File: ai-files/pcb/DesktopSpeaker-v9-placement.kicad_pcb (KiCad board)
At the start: 4 copper layers, 136.9 x 127.8 mm, 351 parts, among them J1 USB_C_Receptacle_USB2.0_16P, J10 B2P-VH, J11 B2P-VH, J2 HEAD_OUT, J3 AUX_IN, J4 I2C service, J5 1S_PACK_3PIN, J6 SWD, J7 SWD_TC2030, J8 BM83_PROG, J9 B2P-VH, Q100 2N7002, Q101 2N7002, Q102 2N7002, Q103 CSD17579Q3A, Q104 2N7002, SW100 WAKE_QON, SW101 BAT_DISCONNECT, SW102 EC11E, U1 BM83SM1-00TA, U10 TPA6132A2RTER, U11 TPS25730DREFR, U12 TPS7A0230PDBVR, U13 TS5A3167DBVR, U14 TPS63802DLAR, U15 TPS63802DLAR, U16 TS5A3167DBVR, U17 TS5A3167DBVR, U19 TPS7B8450QWDRBRQ1, U2 PCM2902CDBR, U20 TPS2116DRLR, U21 TPS3839G33DBZR, U22 TPS7A2033PDBVR, U23 TPS22917DBVR, U24 PCM1862DBTR, U25 TPS61088RHLR, U3 STM32G071RBT6, U4 BQ25792RQMR, U5 MAX17048G+T10, U6 TAS5825MRHBR, U7 TAS5825MRHBR, U8 TS5A23157DGSR, U9 TS5A23157DGSR, Y170 12MHz, Y200 24.576MHz

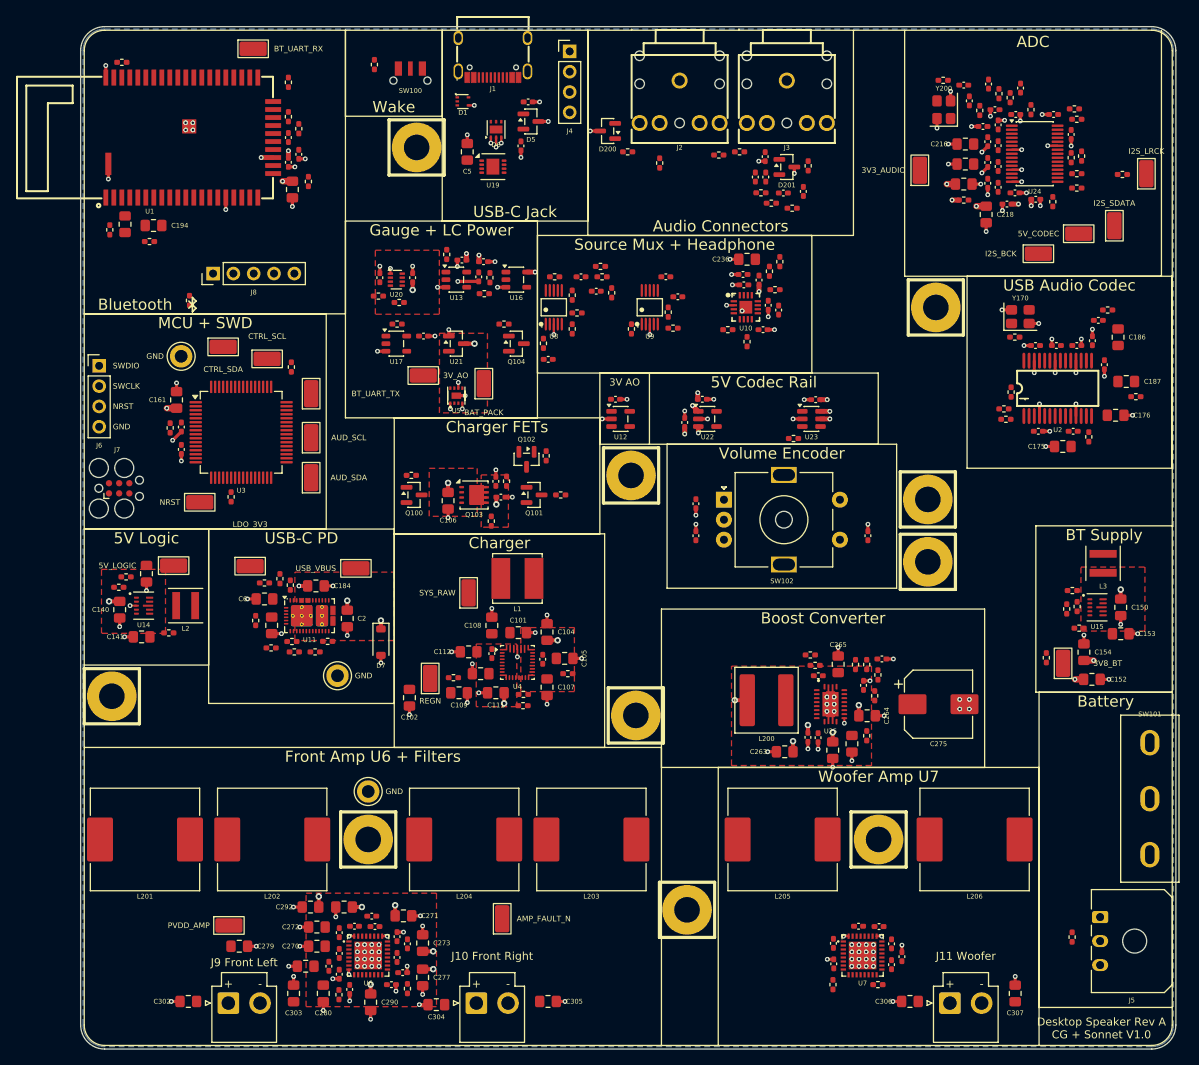
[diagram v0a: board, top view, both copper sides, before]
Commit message: Routing phase 0: GND planes, In2 rail islands, F.Cu pours, 203 GND vias, rail vias; Freerouting trial (draft, not adopted); routing P0 scripts and report
Co-Authored-By: Claude Sonnet 5.5 <noreply@anthropic.com>
Claude-Session: https://claude.ai/code/session_016fe4xPJbEE2SjGafuyNLjb
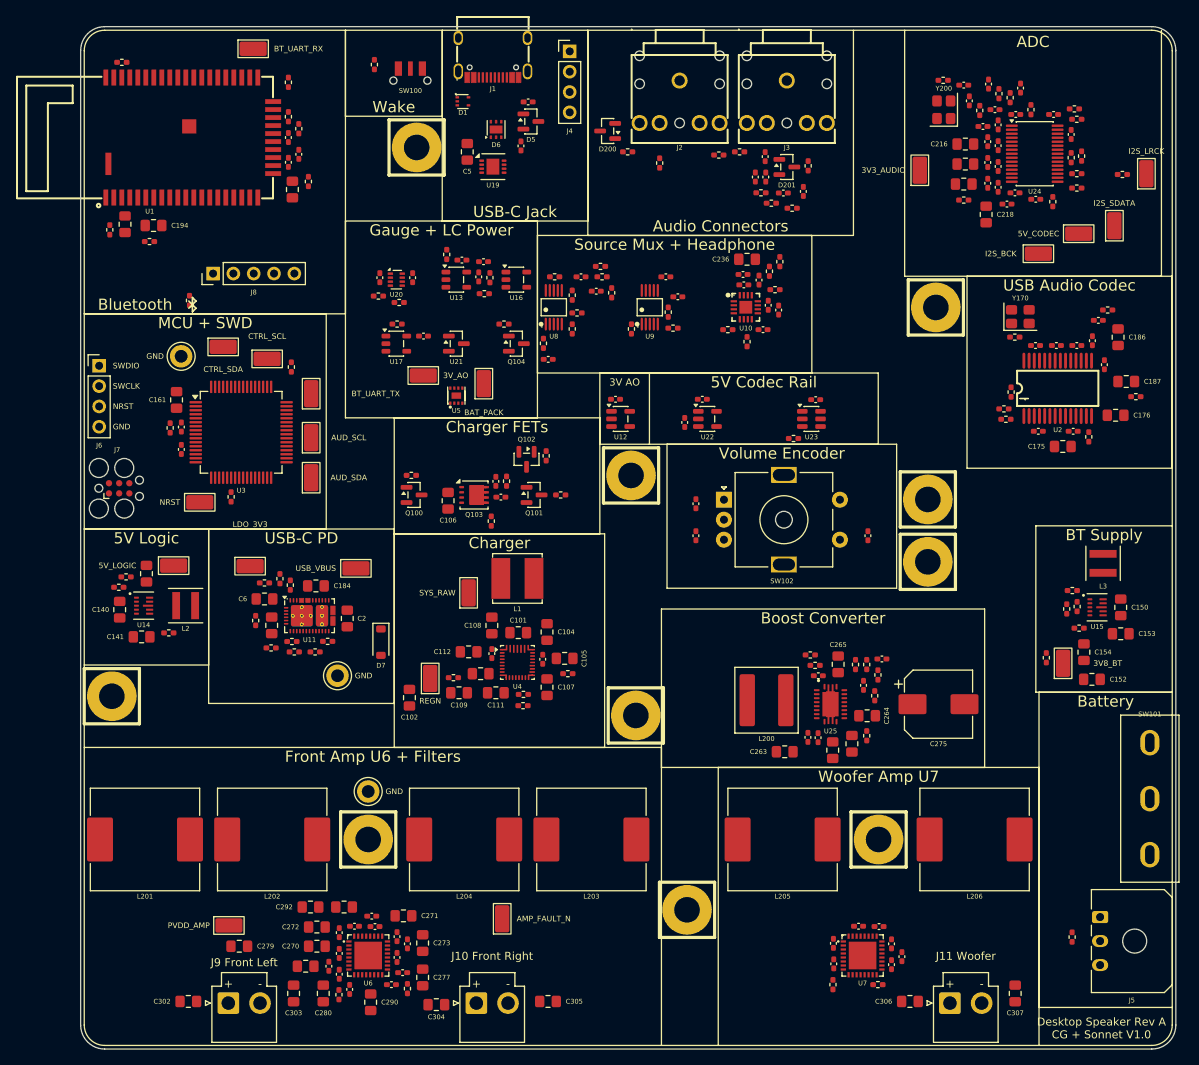
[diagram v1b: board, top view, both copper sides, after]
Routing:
- net GND: track 159.0 -> 0.00 mm, vias 203 -> 0
- net /SYS_RAW: track 11.2 -> 0.00 mm, vias 9 -> 0
- net /Amplifiers/PVDD_AMP: track 7.68 -> 0.00 mm, vias 6 -> 0
- net /3V8_BT: track 5.90 -> 0.00 mm, vias 5 -> 0
- net /3V3_AUDIO: track 5.72 -> 0.00 mm, vias 6 -> 0
- net /3V_AO: track 3.90 -> 0.00 mm, vias 4 -> 0
- net /5V_LOGIC: track 3.50 -> 0.00 mm, vias 4 -> 0
- net /USB_VBUS: track 3.33 -> 0.00 mm, vias 3 -> 0
- net /5V_CODEC: track 3.19 -> 0.00 mm, vias 3 -> 0
- net /Fuel_Gauge_Power/BAT_PACK: track 2.25 -> 0.00 mm, vias 2 -> 0
- net /Battery_Charger/VBUS_PD: track 1.33 -> 0.00 mm, vias 1 -> 0
- net /Battery_Charger/BAT_INT: track 1.19 -> 0.00 mm, vias 1 -> 0
- removed copper zone on In2.Cu, net /3V3_AUDIO
- removed copper zone on In2.Cu, net /3V8_BT
- removed copper zone on In2.Cu, net /3V_AO
- removed copper zone on In2.Cu, net /5V_CODEC
- removed copper zone on In2.Cu, net /5V_LOGIC
- removed copper zone on F.Cu, net /Amplifiers/PVDD_AMP
- removed copper zone on In2.Cu, net /Amplifiers/PVDD_AMP
- removed copper zone on F.Cu, net /Battery_Charger/BAT_INT
- removed copper zone on In2.Cu, net /Battery_Charger/BAT_INT
- removed copper zone on F.Cu, net /Battery_Charger/VBUS_PD
- removed copper zone on In2.Cu, net /Battery_Charger/VBUS_PD
- removed copper zone on F.Cu, net /Fuel_Gauge_Power/BAT_PACK
- removed copper zone on In2.Cu, net /Fuel_Gauge_Power/BAT_PACK
- removed copper zone on F.Cu, net /SYS_RAW
- removed copper zone on In2.Cu, net /SYS_RAW
- removed copper zone on F.Cu, net /USB_VBUS
- removed copper zone on In2.Cu, net /USB_VBUS
- removed copper zone on B.Cu, net GND
- removed copper zone on In1.Cu, net GND
